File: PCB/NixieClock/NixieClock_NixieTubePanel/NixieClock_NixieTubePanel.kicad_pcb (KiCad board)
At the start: 2 copper layers, 112 x 112 mm, 31 parts, among them J3 Conn_01x04_Pin, J4 Conn_01x04_Pin, U1 K155ID1, U2 K155ID1, U3 K155ID1, U4 K155ID1, U5 PCF8574, U6 PCF8574, X1 5230, X2 5230, X3 5230, X4 5230, X5 5230, X6 5230

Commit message: Route tube 4
Finished routing tube 4 top and bottom traces
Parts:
- moved R16 3.54 mm to (168.2, 106.5)
- moved R11 0.75 mm to (140.2, 106.2)
- moved C9 0.11 mm to (148.2, 77.0)
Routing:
- net Net-(N4-'5'): track 3.80 -> 61.3 mm
- net Net-(N4-'6'): track 0.26 -> 54.9 mm
- net Net-(N4-'7'): track 0.95 -> 53.5 mm
- net Net-(N4-'8'): track 0.00 -> 47.1 mm
- net Net-(N4-'2'): track 0.00 -> 42.4 mm, vias 0 -> 1
- net Net-(N4-'1'): track 0.00 -> 33.3 mm
- net Net-(N4-'4'): track 2.65 -> 35.2 mm
- net GND: track 44.3 -> 66.5 mm, vias 8 -> 7
- net Net-(N4-'3'): track 2.27 -> 23.0 mm
- net Net-(N4-'9'): track 0.00 -> 20.1 mm
- net Net-(N4-'0'): track 0.00 -> 13.7 mm
- net +5V: track 211.6 -> 205.4 mm, vias 5 -> 4
- net /+170V: track 75.4 -> 78.9 mm, vias 5 -> 7
- net Net-(N4-V+): track 8.34 -> 6.24 mm
- net Net-(J3-Pin_4): track 56.1 -> 54.7 mm
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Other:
- board text added: "okay to add teardrops"

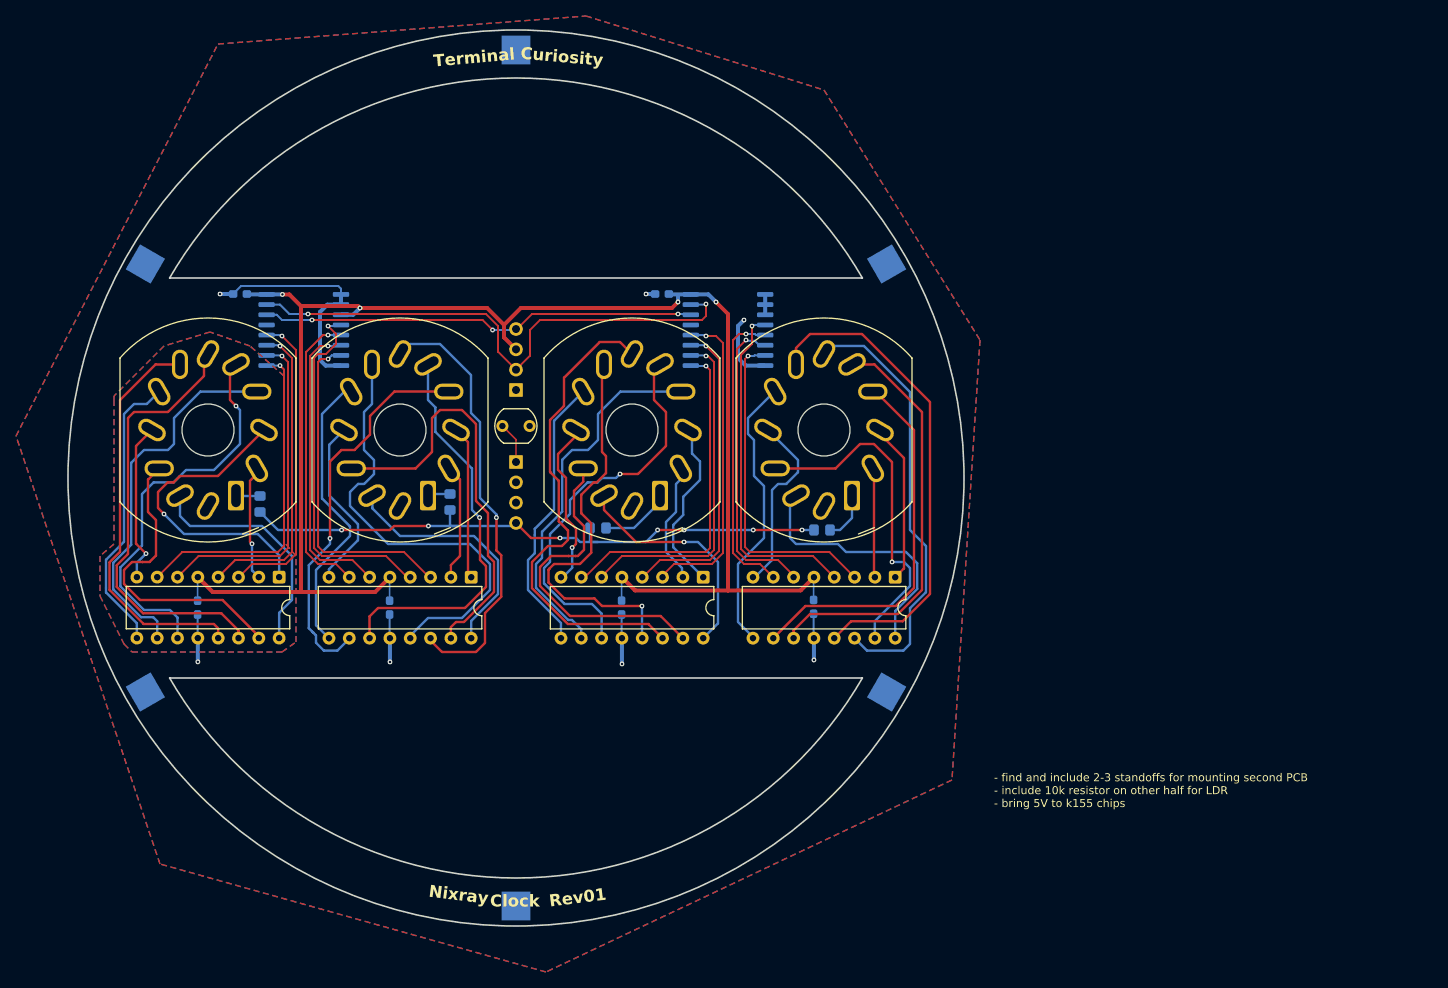
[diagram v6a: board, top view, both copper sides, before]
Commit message: add Polygon pour + stitching vias
Add polygon ground pour to top and bottom. add stitching vias all around board for improved layer connection. add polygon keepout zones to keep ground plane away from HV components
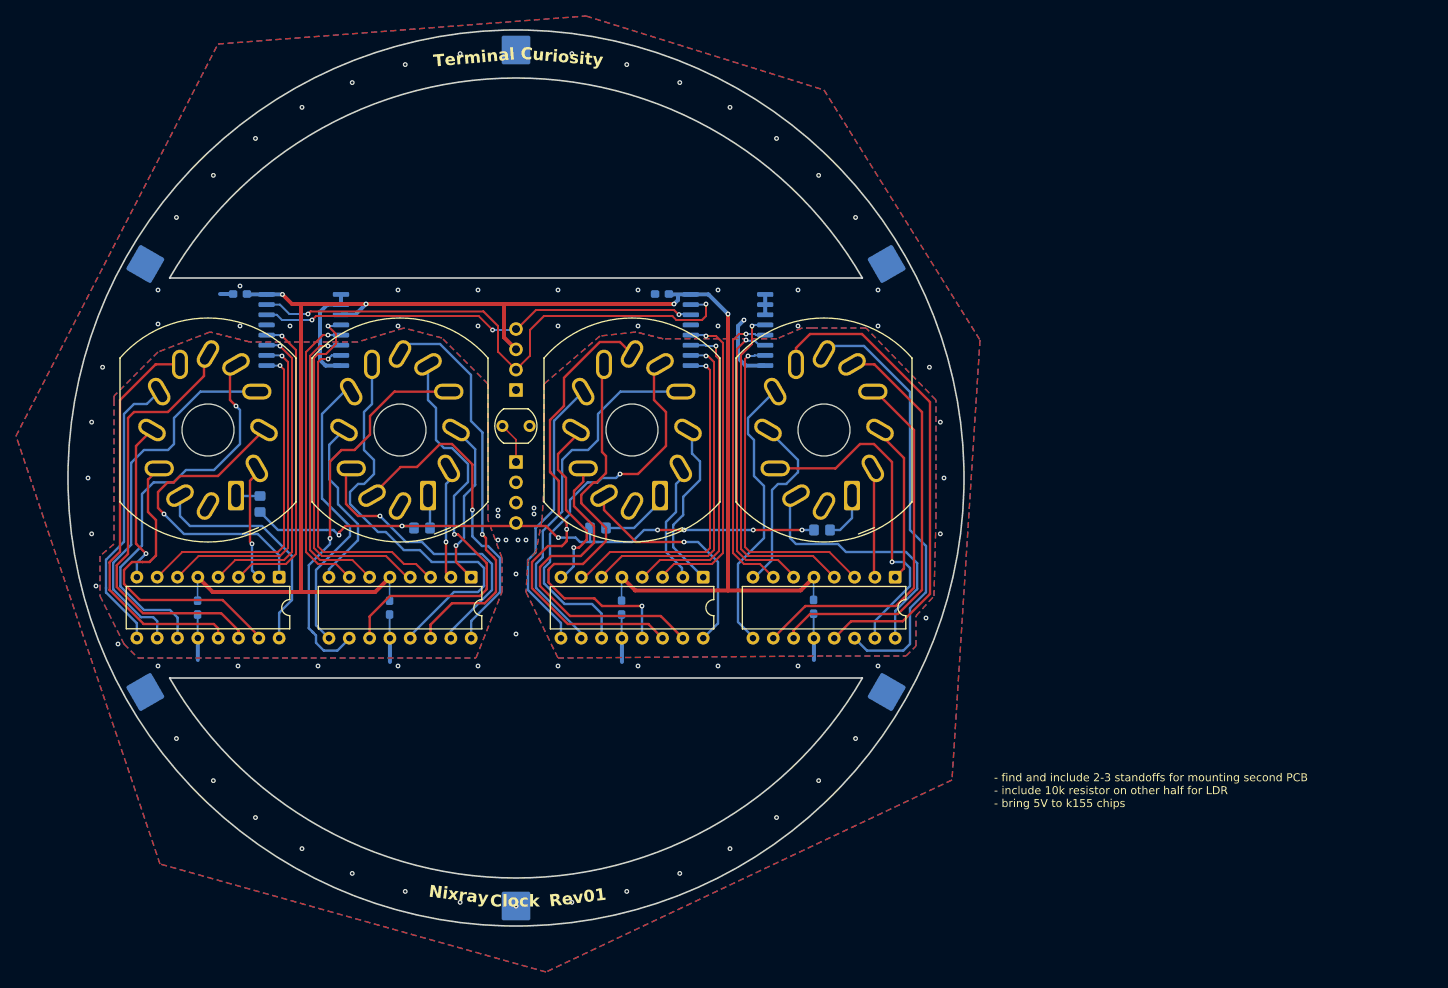
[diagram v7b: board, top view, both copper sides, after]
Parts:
- moved R10 4.78 mm to (118.2, 106.2), turned to 180 degrees
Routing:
- net GND: track 66.5 -> 50.0 mm, vias 7 -> 80
- net Net-(N2-'2'): track 52.4 -> 37.5 mm, vias 0 -> 1
- net Net-(N2-'1'): track 31.2 -> 41.4 mm, vias 0 -> 1
- net Net-(N2-'6'): track 56.2 -> 52.2 mm
- net Net-(N2-'7'): track 49.6 -> 52.2 mm
- net Net-(N2-'5'): track 56.7 -> 54.5 mm
- net Net-(N2-'9'): track 19.6 -> 21.7 mm, vias 0 -> 1
- net Net-(N3-'5'): track 51.1 -> 52.8 mm
- net +5V: track 205.4 -> 207.0 mm
- net Net-(N3-'3'): track 21.2 -> 22.7 mm
- net Net-(N3-'2'): track 40.5 -> 41.8 mm
- net Net-(J3-Pin_4): track 54.7 -> 55.6 mm
- net Net-(N2-V+): track 2.83 -> 3.65 mm
- net Net-(U3-D): track 39.2 -> 40.0 mm
- net Net-(J3-Pin_2): track 68.3 -> 68.9 mm
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
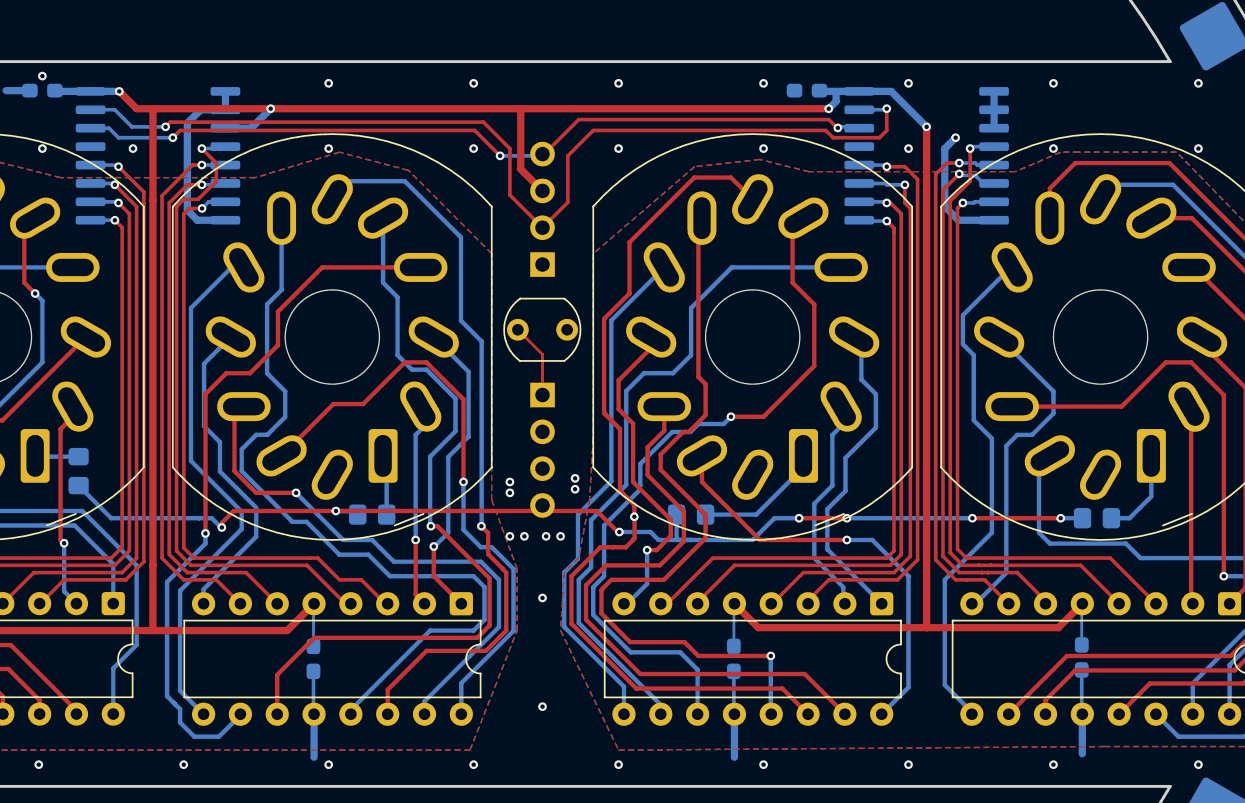
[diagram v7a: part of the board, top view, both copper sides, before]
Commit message: mid-DRC review
mid review checkpoint. errors require reloading footprints from library, which might break a lot of things. This checkpoint captures last good state
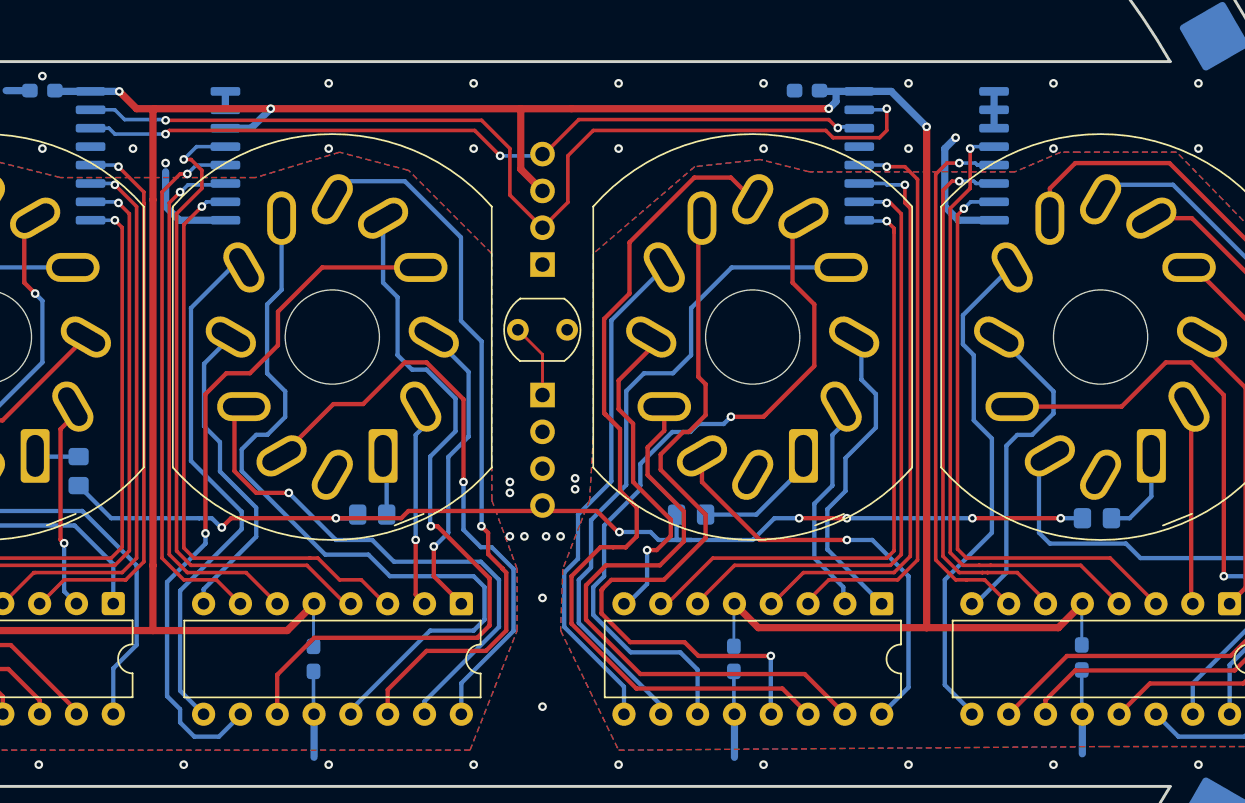
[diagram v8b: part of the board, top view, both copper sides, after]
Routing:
- net GND: track 50.0 -> 45.0 mm, vias 80 -> 81
- net Net-(U4-B): track 38.0 -> 38.6 mm
- net Net-(N3-'6'): track 60.6 -> 60.7 mm, vias 1 -> 0
